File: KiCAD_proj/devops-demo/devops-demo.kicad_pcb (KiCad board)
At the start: 2 copper layers, 52.7 x 36.8 mm, 13 parts, among them J1 Conn_PinHeader_FTDI_1x06_P2.5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, SW1 SWITCH_JS102011JCQN, SW2 BUTTON_B3SN, U1 ESP32-WROOM-32, U2 AMS1117-3.3

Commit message: Routed
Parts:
- added C4: 0.1uF, fab:C_1206, F.Cu at (148.0, 113.1)
- C3: value 0.1uF -> 10uF
- moved R1 16.3 mm to (161.3, 101.0), turned to 90 degrees
- moved D1 7.78 mm to (161.3, 107.9), turned to 90 degrees
- moved J1 2.54 mm to (168.9, 93.3)
- moved C2 0.90 mm to (154.8, 95.2)
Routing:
- net GND: track 0.00 -> 131.3 mm
- net RXI: track 0.00 -> 75.9 mm
- net TXO: track 0.00 -> 68.9 mm
- net +3V3: track 0.00 -> 51.8 mm
- net VCC: track 0.00 -> 26.9 mm
- net EN: track 0.00 -> 21.6 mm
- net IO0: track 0.00 -> 11.0 mm
- net IO2: track 0.00 -> 4.46 mm
- net Net-(D2-Pad2): track 0.00 -> 3.62 mm
- net Net-(D1-Pad2): track 0.00 -> 2.89 mm
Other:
- board size 52.7 x 36.8 mm -> 52.7 x 41.3 mm

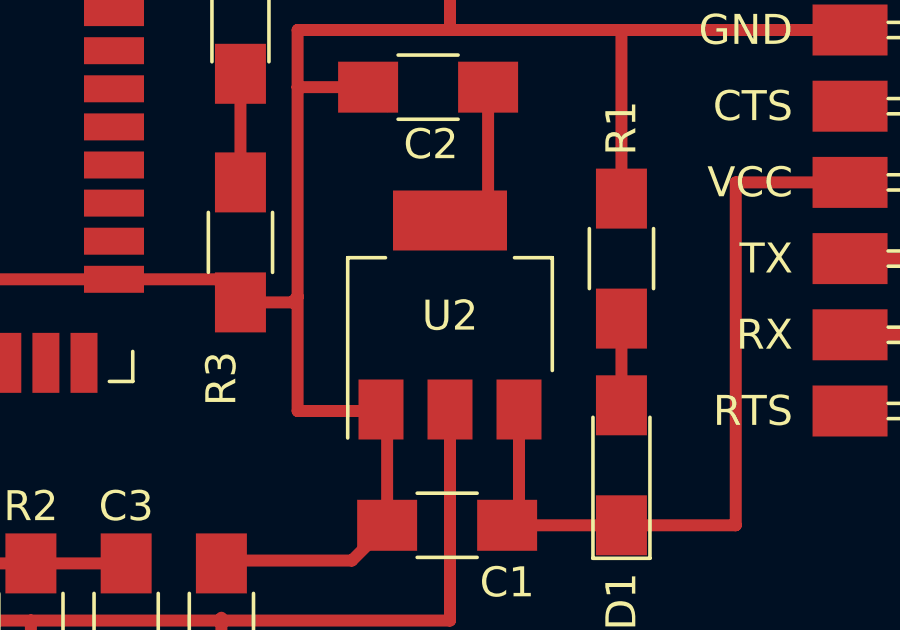
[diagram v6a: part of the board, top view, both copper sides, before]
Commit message: added missing trace in AMS1117
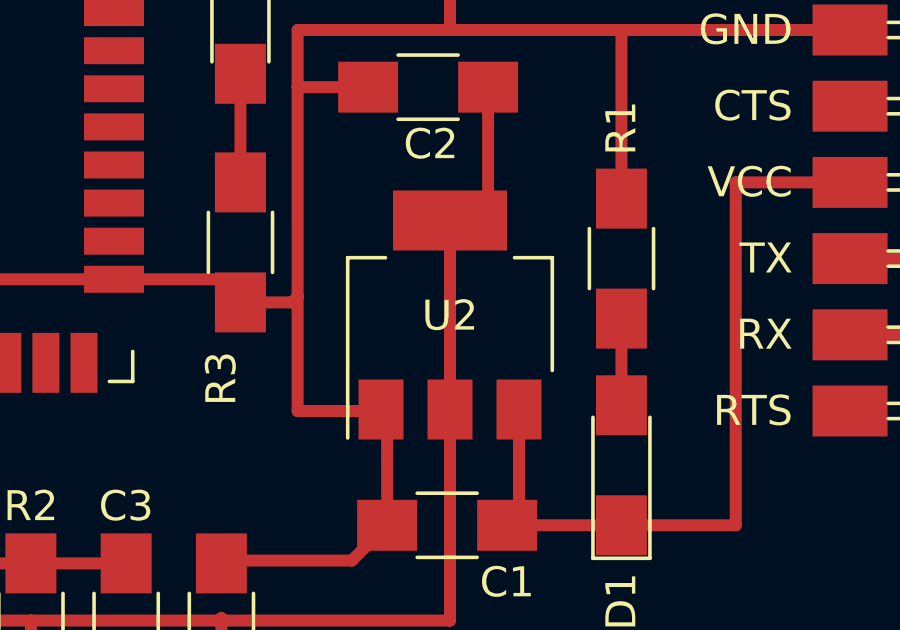
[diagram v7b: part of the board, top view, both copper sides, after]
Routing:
- net +3V3: track 51.8 -> 58.1 mm
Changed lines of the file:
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@@
     (thickness 1.6)
     (drawings 7)
-    (tracks 76)
+    (tracks 77)
     (zones 0)
     (modules 14)
@@
   (segment (start 156.845 95.25) (end 156.845 99.06) (width 0.4) (layer F.Cu) (net 2))
   (segment (start 156.21 99.06) (end 155.575 99.695) (width 0.4) (layer F.Cu) (net 2))
+  (segment (start 155.575 105.995) (end 155.575 99.695) (width 0.4) (layer F.Cu) (net 2))
   (segment (start 161.29 102.965) (end 161.29 105.855) (width 0.4) (layer F.Cu) (net 3))
   (segment (start 129.405 110.37) (end 130.16 111.125) (width 0.4) (layer F.Cu) (net 35))

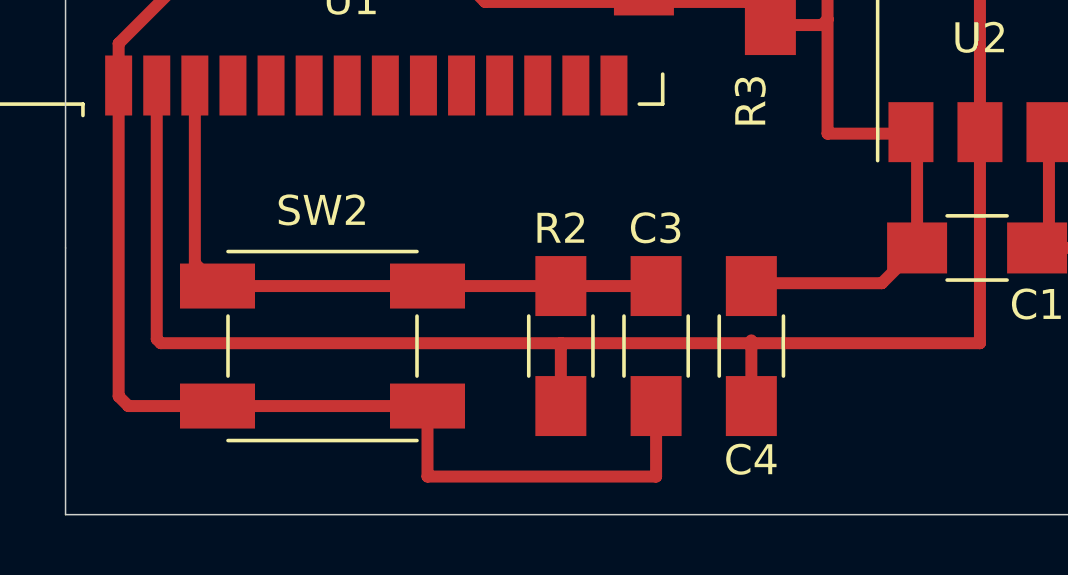
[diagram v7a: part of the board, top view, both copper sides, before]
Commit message: added extra clearance for 3V3
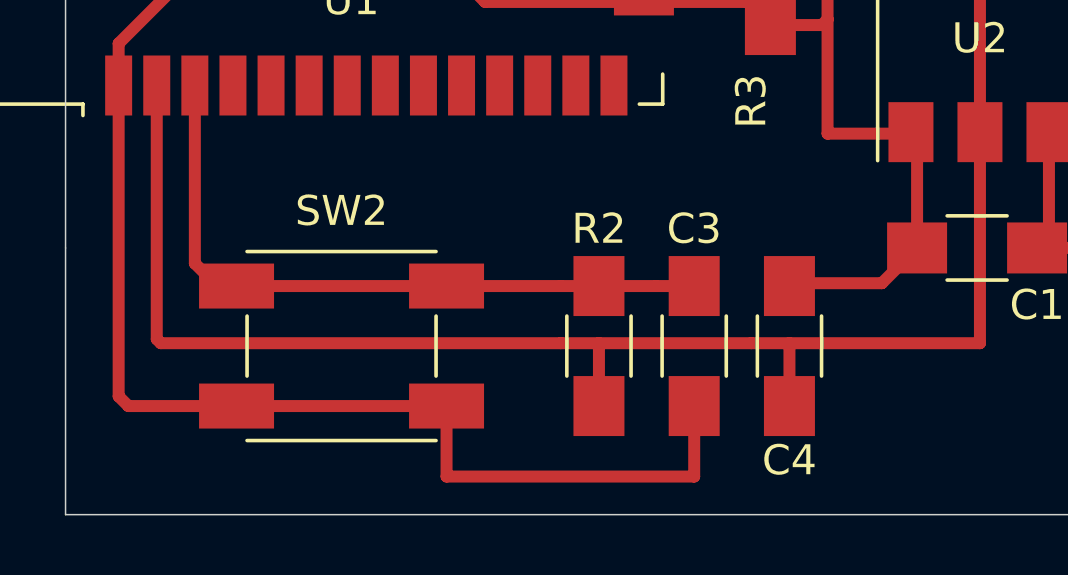
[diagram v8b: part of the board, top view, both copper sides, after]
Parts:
- moved C3 1.27 mm to (146.1, 113.1)
- moved R2 1.27 mm to (142.9, 113.1)
- moved C4 1.27 mm to (149.2, 113.1)
- moved SW2 0.63 mm to (134.3, 113.1)
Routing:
- net EN: track 21.6 -> 22.9 mm
- net GND: track 131.3 -> 130.7 mm
